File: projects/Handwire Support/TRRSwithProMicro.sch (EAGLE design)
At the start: 5 parts, among them SW1 RSTSWSMD

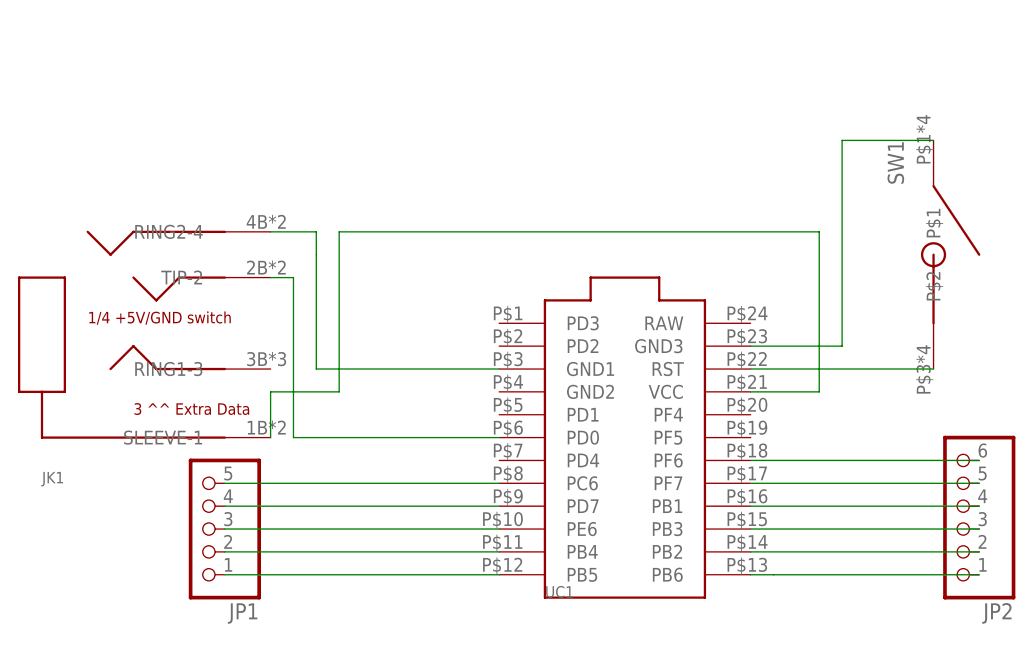
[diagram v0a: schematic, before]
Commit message: Reversible handwires
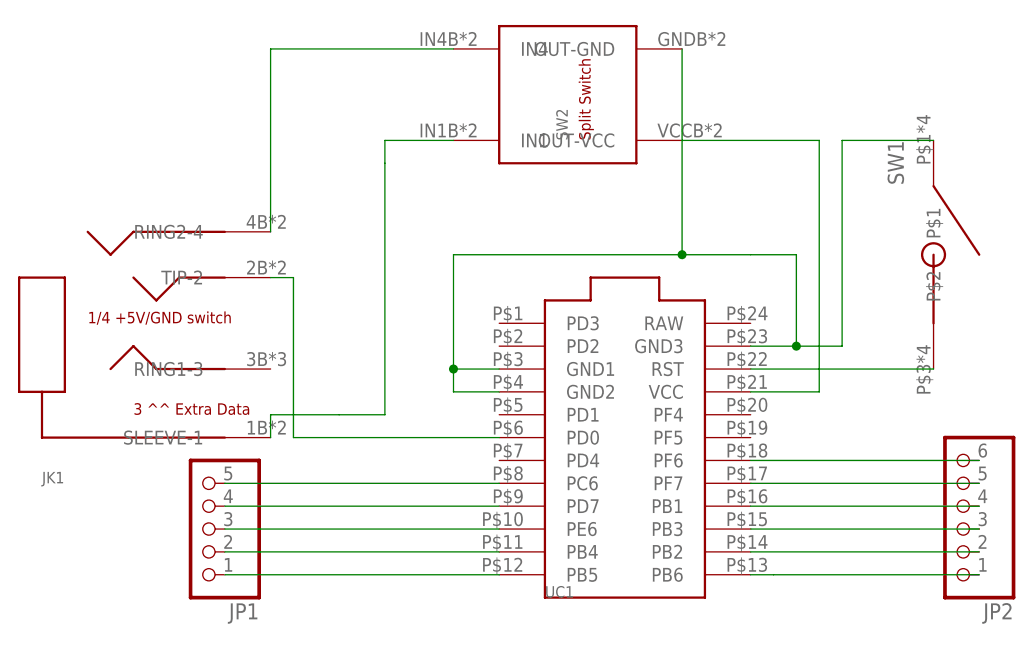
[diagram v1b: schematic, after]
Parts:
- added SW2: TRANSFERPADDY, Keys:TRANSFERPADDY
- JK1: value TRRSJACK -> TRRSJACKOVER; device Keys:TRRSJACK -> Keys:TRRSJACKOVER
- UC1: value PROMICROUNDER -> PROMICROTOP; device Keys:PROMICROUNDER -> Keys:PROMICROTOP
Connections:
- new net N$17: SW2.OUT-VCC, UC1.VCC
- net N$1: now also SW2.IN1; no longer UC1.VCC
- net N$2: now also SW1.P$1, SW2.OUT-GND, UC1.GND2, UC1.GND3; no longer JK1.RING2-4
- net N$4: now also JK1.RING2-4, SW2.IN4; no longer SW1.P$1, UC1.GND3
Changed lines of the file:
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@@
 </classes>
 <parts>
-<part name="UC1" library="Keys" library_urn="urn:adsk.eagle:library:1331239" deviceset="PROMICRO" device="UNDER" package3d_urn="urn:adsk.eagle:package:1399517/9" value="PROMICROUNDER"/>
-<part name="JK1" library="Keys" library_urn="urn:adsk.eagle:library:1331239" deviceset="TRRSJACK" device="" package3d_urn="urn:adsk.eagle:package:1393948/13"/>
+<part name="UC1" library="Keys" library_urn="urn:adsk.eagle:library:1331239" deviceset="PROMICRO" device="TOP" package3d_urn="urn:adsk.eagle:package:1331250/10" value="PROMICROTOP"/>
+<part name="JK1" library="Keys" library_urn="urn:adsk.eagle:library:1331239" deviceset="TRRSJACK" device="OVER"/>
 <part name="SW1" library="Keys" library_urn="urn:adsk.eagle:library:1331239" deviceset="RSTSW" device="SMD" package3d_urn="urn:adsk.eagle:package:1393947/7"/>
 <part name="JP1" library="pinhead" library_urn="urn:adsk.eagle:library:325" deviceset="PINHD-1X5" device="" package3d_urn="urn:adsk.eagle:package:22469/2"/>
 <part name="JP2" library="pinhead" library_urn="urn:adsk.eagle:library:325" deviceset="PINHD-1X6" device="" package3d_urn="urn:adsk.eagle:package:22472/2"/>
+<part name="SW2" library="Keys" library_urn="urn:adsk.eagle:library:1331239" deviceset="TRANSFER" device="PADDY" package3d_urn="urn:adsk.eagle:package:3624143/2"/>
 </parts>
 <sheets>
@@
 <instance part="JP1" gate="A" x="17.78" y="27.94" rot="R180"/>
 <instance part="JP2" gate="A" x="101.6" y="30.48" rot="R180"/>
+<instance part="SW2" gate="G$1" x="58.42" y="76.2" rot="R90"/>
 </instances>
 <busses>
 </busses>
 <nets>
-<net name="N$1" class="0">
-<segment>
-<pinref part="JK1" gate="G$1" pin="SLEEVE-1"/>
-<wire x1="25.4" y1="43.18" x2="25.4" y2="38.1" width="0.1524" layer="91"/>
-<wire x1="25.4" y1="43.18" x2="33.02" y2="43.18" width="0.1524" layer="91"/>
-<wire x1="86.36" y1="60.96" x2="86.36" y2="43.18" width="0.1524" layer="91"/>
-<pinref part="UC1" gate="G$1" pin="VCC"/>
-<wire x1="86.36" y1="43.18" x2="78.74" y2="43.18" width="0.1524" layer="91"/>
-<wire x1="33.02" y1="43.18" x2="33.02" y2="60.96" width="0.1524" layer="91"/>
-<wire x1="33.02" y1="60.96" x2="86.36" y2="60.96" width="0.1524" layer="91"/>
-</segment>
-</net>
 <net name="N$3" class="0">
 <segment>
@@
 <pinref part="UC1" gate="G$1" pin="PD0"/>
 <wire x1="27.94" y1="38.1" x2="50.8" y2="38.1" width="0.1524" layer="91"/>
-</segment>
-</net>
-<net name="N$4" class="0">
-<segment>
-<pinref part="UC1" gate="G$1" pin="GND3"/>
-<wire x1="78.74" y1="48.26" x2="88.9" y2="48.26" width="0.1524" layer="91"/>
-<pinref part="SW1" gate="G$1" pin="P$1"/>
-<wire x1="88.9" y1="48.26" x2="88.9" y2="71.12" width="0.1524" layer="91"/>
-<wire x1="88.9" y1="71.12" x2="99.06" y2="71.12" width="0.1524" layer="91"/>
 </segment>
 </net>
@@
 <net name="N$2" class="0">
 <segment>
-<pinref part="JK1" gate="G$1" pin="RING2-4"/>
-<wire x1="25.4" y1="60.96" x2="30.48" y2="60.96" width="0.1524" layer="91"/>
-<wire x1="30.48" y1="60.96" x2="30.48" y2="58.42" width="0.1524" layer="91"/>
 <pinref part="UC1" gate="G$1" pin="GND1"/>
-<wire x1="30.48" y1="58.42" x2="30.48" y2="45.72" width="0.1524" layer="91"/>
-<wire x1="30.48" y1="45.72" x2="50.8" y2="45.72" width="0.1524" layer="91"/>
+<pinref part="UC1" gate="G$1" pin="GND2"/>
+<wire x1="45.72" y1="45.72" x2="50.8" y2="45.72" width="0.1524" layer="91"/>
+<wire x1="50.8" y1="43.18" x2="45.72" y2="43.18" width="0.1524" layer="91"/>
+<wire x1="45.72" y1="43.18" x2="45.72" y2="45.72" width="0.1524" layer="91"/>
+<junction x="45.72" y="45.72"/>
+<wire x1="45.72" y1="45.72" x2="45.72" y2="58.42" width="0.1524" layer="91"/>
+<wire x1="45.72" y1="58.42" x2="71.12" y2="58.42" width="0.1524" layer="91"/>
+<pinref part="UC1" gate="G$1" pin="GND3"/>
+<wire x1="71.12" y1="58.42" x2="78.74" y2="58.42" width="0.1524" layer="91"/>
+<wire x1="78.74" y1="48.26" x2="83.82" y2="48.26" width="0.1524" layer="91"/>
+<pinref part="SW1" gate="G$1" pin="P$1"/>
+<wire x1="83.82" y1="48.26" x2="88.9" y2="48.26" width="0.1524" layer="91"/>
+<wire x1="88.9" y1="48.26" x2="88.9" y2="71.12" width="0.1524" layer="91"/>
+<wire x1="88.9" y1="71.12" x2="99.06" y2="71.12" width="0.1524" layer="91"/>
+<wire x1="78.74" y1="58.42" x2="83.82" y2="58.42" width="0.1524" layer="91"/>
+<wire x1="83.82" y1="58.42" x2="83.82" y2="48.26" width="0.1524" layer="91"/>
+<junction x="83.82" y="48.26"/>
+<pinref part="SW2" gate="G$1" pin="OUT-GND"/>
+<wire x1="71.12" y1="81.28" x2="71.12" y2="58.42" width="0.1524" layer="91"/>
+<junction x="71.12" y="58.42"/>
 </segment>
 </net>
+<net name="N$1" class="0">
+<segment>
+<pinref part="JK1" gate="G$1" pin="SLEEVE-1"/>
+<wire x1="25.4" y1="38.1" x2="25.4" y2="40.64" width="0.1524" layer="91"/>
+<wire x1="25.4" y1="40.64" x2="33.02" y2="40.64" width="0.1524" layer="91"/>
+<wire x1="33.02" y1="40.64" x2="38.1" y2="40.64" width="0.1524" layer="91"/>
+<wire x1="38.1" y1="40.64" x2="38.1" y2="68.58" width="0.1524" layer="91"/>
+<pinref part="SW2" gate="G$1" pin="IN1"/>
+<wire x1="38.1" y1="68.58" x2="38.1" y2="71.12" width="0.1524" layer="91"/>
+<wire x1="38.1" y1="71.12" x2="45.72" y2="71.12" width="0.1524" layer="91"/>
+</segment>
+</net>
+<net name="N$4" class="0">
+<segment>
+<pinref part="JK1" gate="G$1" pin="RING2-4"/>
+<pinref part="SW2" gate="G$1" pin="IN4"/>
+<wire x1="25.4" y1="60.96" x2="25.4" y2="81.28" width="0.1524" layer="91"/>
+<wire x1="25.4" y1="81.28" x2="45.72" y2="81.28" width="0.1524" layer="91"/>
+</segment>
+</net>
+<net name="N$17" class="0">
+<segment>
+<pinref part="SW2" gate="G$1" pin="OUT-VCC"/>
+<wire x1="71.12" y1="71.12" x2="86.36" y2="71.12" width="0.1524" layer="91"/>
+<wire x1="86.36" y1="71.12" x2="86.36" y2="43.18" width="0.1524" layer="91"/>
+<pinref part="UC1" gate="G$1" pin="VCC"/>
+<wire x1="86.36" y1="43.18" x2="78.74" y2="43.18" width="0.1524" layer="91"/>
+</segment>
+</net>
